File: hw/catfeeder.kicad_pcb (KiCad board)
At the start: 2 copper layers, 56 x 55.2 mm, 15 parts, among them IC1 ATMEGA328-P, P1 LCD, P2 PROG, P3 SERVO, P4 3_3_SUP, P5 ROT_SWITCH, P6 CONN_01X06, P7 BUTTON, P8 HC-SR04, P9 WS2812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

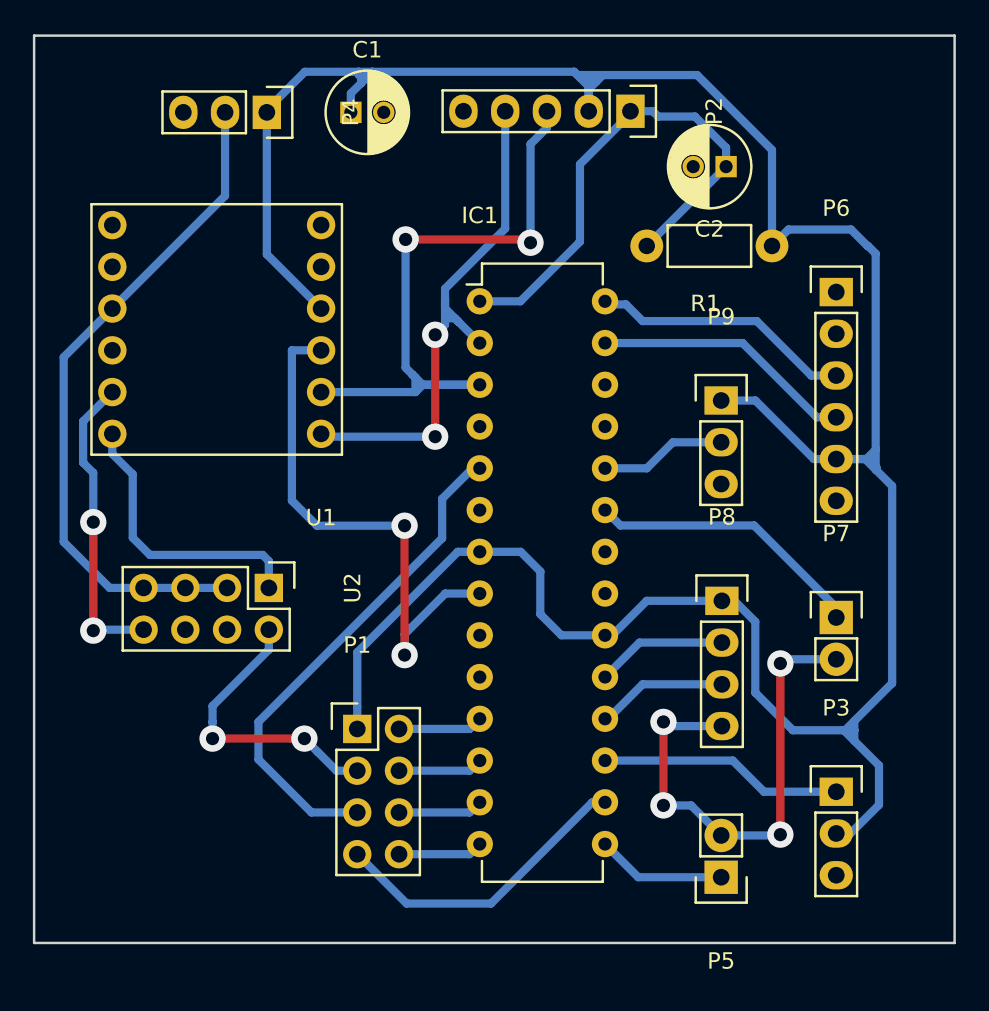
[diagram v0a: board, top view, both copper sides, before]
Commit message: Modify schematic to avoid gnd via
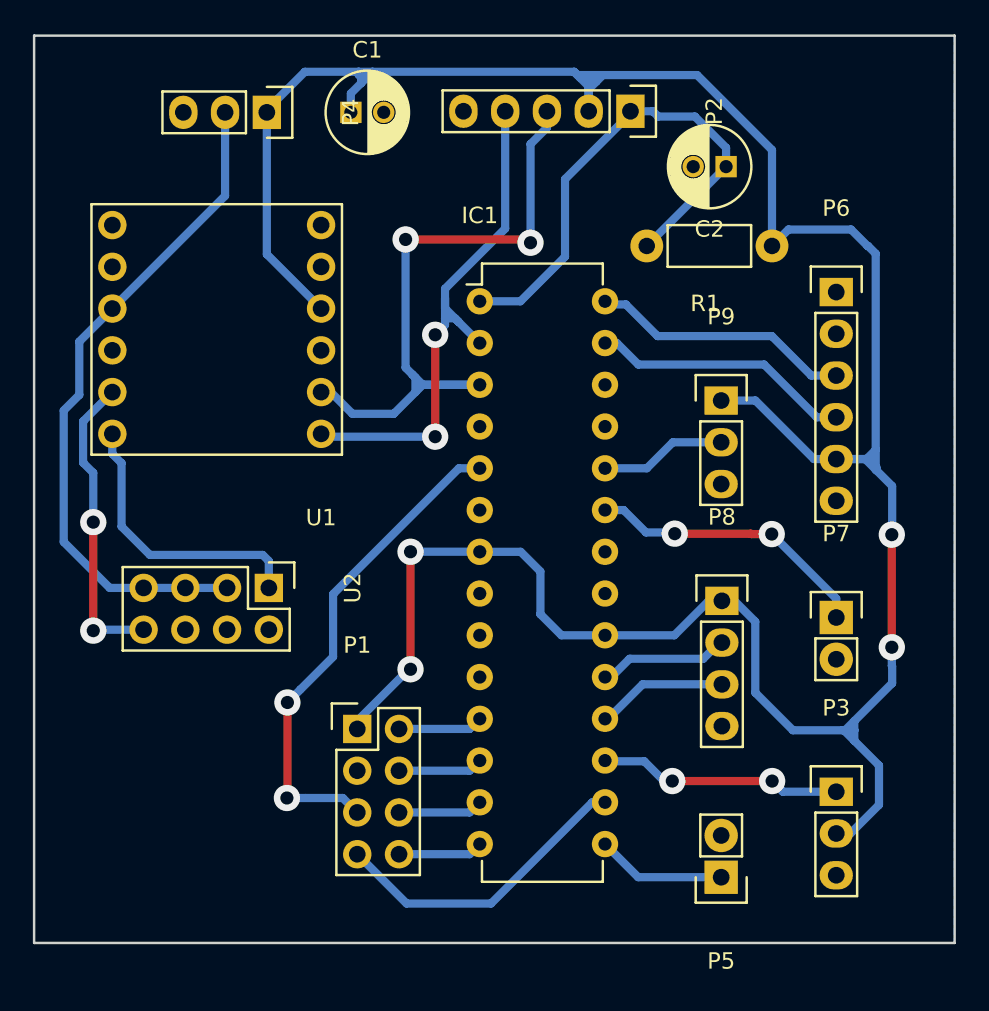
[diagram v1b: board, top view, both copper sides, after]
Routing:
- net GND: track 81.4 -> 0.00 mm, vias 8 -> 0
- net +5V: track 173.7 -> 175.5 mm, vias 0 -> 4
- net /ATMEGA_TX: track 39.9 -> 41.0 mm
- net /BUTTON: track 17.7 -> 18.6 mm, vias 0 -> 2
- net /REG_SEL: track 30.9 -> 30.3 mm, vias 0 -> 2
- net /SERVO: vias 0 -> 2

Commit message: Update catfeeder schematics
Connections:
- U2 pad 4: (no net) -> /RESET
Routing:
- net /RESET: track 31.5 -> 100.6 mm, vias 0 -> 4
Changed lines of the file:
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@@
 (kicad_pcb (version 4) (host pcbnew "(2016-05-03 BZR 6770, Git 22c4e4d)-product")
   (general
-    (links 53)
-    (no_connects 0)
-    (area 81.524999 56.5105 149.000001 114.600001)
+    (links 54)
+    (no_connects 16)
+    (area 81.524999 56.724999 137.675001 112.075001)
     (thickness 1.6)
     (drawings 5)
-    (tracks 232)
+    (tracks 254)
     (zones 0)
     (modules 15)
@@
     (pad 3 thru_hole oval (at 0 2.54 270) (size 1.7272 1.7272) (drill 1.016) (layers *.Cu *.Mask F.SilkS)
       (net 16 +3V3))
-    (pad 4 thru_hole oval (at 2.54 2.54 270) (size 1.7272 1.7272) (drill 1.016) (layers *.Cu *.Mask F.SilkS))
+    (pad 4 thru_hole oval (at 2.54 2.54 270) (size 1.7272 1.7272) (drill 1.016) (layers *.Cu *.Mask F.SilkS)
+      (net 3 /RESET))
     (pad 5 thru_hole oval (at 0 5.08 270) (size 1.7272 1.7272) (drill 1.016) (layers *.Cu *.Mask F.SilkS)
       (net 16 +3V3))
@@
   (segment (start 111.203047 88.203047) (end 108.712418 88.203047) (width 0.5) (layer B.Cu) (net 1))
   (segment (start 115.34 61.4) (end 115.34 60.06) (width 0.5) (layer B.Cu) (net 1))
+  (segment (start 93.34 92.94) (end 92.476401 93.803599) (width 0.5) (layer B.Cu) (net 3))
+  (segment (start 92.476401 93.803599) (end 92.476401 93.963599) (width 0.5) (layer B.Cu) (net 3))
+  (segment (start 92.476401 93.963599) (end 91.36 95.08) (width 0.5) (layer B.Cu) (net 3))
+  (segment (start 91.36 95.08) (end 85.133998 95.08) (width 0.5) (layer B.Cu) (net 3))
+  (segment (start 85.133998 95.08) (end 82.49 92.436002) (width 0.5) (layer B.Cu) (net 3))
+  (segment (start 82.49 92.436002) (end 82.49 74.52) (width 0.5) (layer B.Cu) (net 3))
+  (segment (start 82.49 74.52) (end 84.17 72.84) (width 0.5) (layer B.Cu) (net 3))
+  (segment (start 85.46 66.08) (end 90.52 66.08) (width 0.5) (layer B.Cu) (net 3))
+  (segment (start 84.17 72.84) (end 84.17 67.37) (width 0.5) (layer B.Cu) (net 3))
+  (segment (start 84.17 67.37) (end 85.46 66.08) (width 0.5) (layer B.Cu) (net 3))
+  (segment (start 90.52 66.08) (end 90.63 66.19) (width 0.5) (layer B.Cu) (net 3))
+  (segment (start 97.76 66.04) (end 106.22 66.04) (width 0.5) (layer B.Cu) (net 3))
+  (segment (start 106.3 66.04) (end 106.26 66) (width 0.5) (layer F.Cu) (net 3))
+  (segment (start 106.22 66.04) (end 106.26 66) (width 0.5) (layer B.Cu) (net 3))
+  (segment (start 113.9 66.04) (end 106.3 66.04) (width 0.5) (layer F.Cu) (net 3))
+  (via (at 106.26 66) (size 1.6) (drill 0.8) (layers F.Cu B.Cu) (net 3))
+  (segment (start 113.9 70.25) (end 113.9 66.04) (width 0.5) (layer B.Cu) (net 3))
+  (segment (start 113.9 66.04) (end 113.9 65.5324) (width 0.5) (layer B.Cu) (net 3))
+  (via (at 113.9 66.04) (size 1.6) (drill 0.8) (layers F.Cu B.Cu) (net 3))
+  (segment (start 90.63 66.19) (end 97.61 66.19) (width 0.5) (layer F.Cu) (net 3))
+  (segment (start 97.61 66.19) (end 97.76 66.04) (width 0.5) (layer F.Cu) (net 3))
+  (via (at 97.76 66.04) (size 1.6) (drill 0.8) (layers F.Cu B.Cu) (net 3))
+  (via (at 90.63 66.19) (size 1.6) (drill 0.8) (layers F.Cu B.Cu) (net 3))
   (segment (start 108.712418 72.963047) (end 111.186953 72.963047) (width 0.5) (layer B.Cu) (net 3))
   (segment (start 111.186953 72.963047) (end 113.9 70.25) (width 0.5) (layer B.Cu) (net 3))
-  (segment (start 113.9 70.25) (end 113.9 65.5324) (width 0.5) (layer B.Cu) (net 3))
   (segment (start 113.9 65.5324) (end 117.88 61.5524) (width 0.5) (layer B.Cu) (net 3))
   (segment (start 117.88 61.5524) (end 117.88 61.4) (width 0.5) (layer B.Cu) (net 3))
